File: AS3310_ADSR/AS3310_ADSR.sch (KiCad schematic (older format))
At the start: 26 parts, among them J1 ADSR_Pots, J2 Gate, J3 Peak, J4 AtkOut, J5 EnvOut, J6 Trigger, J7 Power, U1 AS3310, U2 TL071

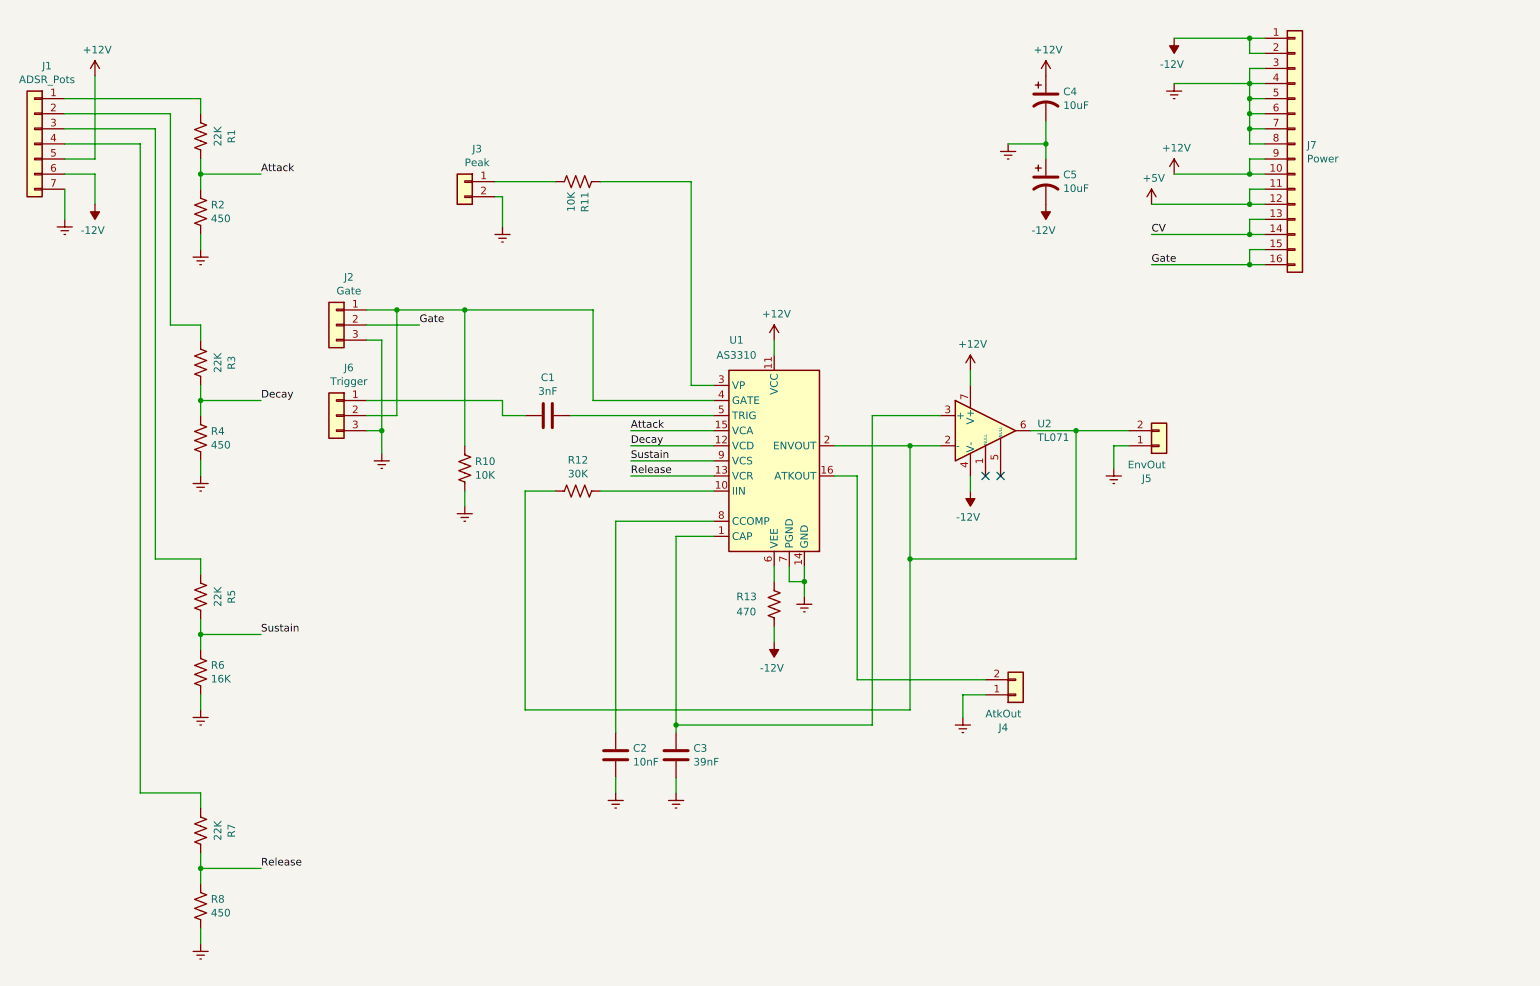
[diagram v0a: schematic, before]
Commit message: Combine IO and main ADSR boards
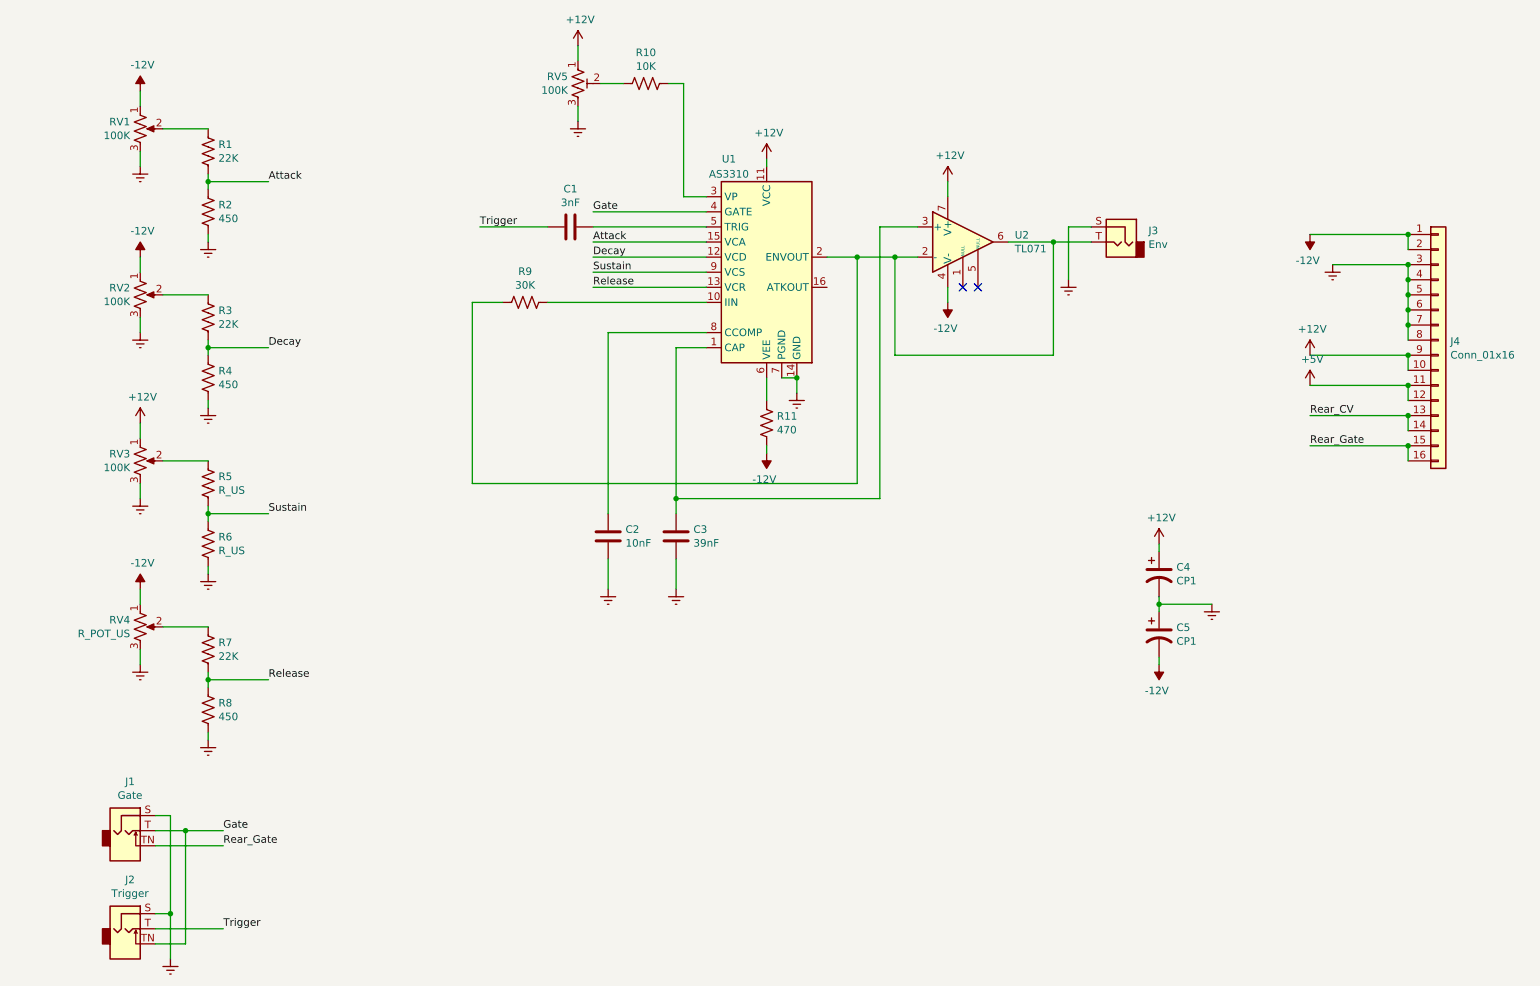
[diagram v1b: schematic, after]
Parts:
- removed J1: ADSR_Pots, Connector_PinHeader_2.54mm:PinHeader_1x07_P2.54mm_Vertical, symbol Connector_Generic:Conn_01x07
- removed J2: Gate, Connector_PinHeader_2.54mm:PinHeader_1x03_P2.54mm_Vertical, symbol Connector_Generic:Conn_01x03
- removed J3: Peak, Connector_PinHeader_2.54mm:PinHeader_1x02_P2.54mm_Vertical, symbol Connector_Generic:Conn_01x02
- removed J4: AtkOut, Connector_PinHeader_2.54mm:PinHeader_1x02_P2.54mm_Vertical, symbol Connector_Generic:Conn_01x02
- removed J5: EnvOut, Connector_PinHeader_2.54mm:PinHeader_1x02_P2.54mm_Vertical, symbol Connector_Generic:Conn_01x02
- removed J6: Trigger, Connector_PinHeader_2.54mm:PinHeader_1x03_P2.54mm_Vertical, symbol Connector_Generic:Conn_01x03
- removed J7: Power, Connector_IDC:IDC-Header_2x08_P2.54mm_Vertical, symbol Connector_Generic:Conn_01x16
- removed R12: 30K, Resistor_SMD:R_0805_2012Metric, symbol Device:R_US
- removed R13: 470, Resistor_SMD:R_0805_2012Metric, symbol Device:R_US
- added J1: Gate, Eurorack:Jack_3.5mm_QingPu_WQP-PJ398SM_Vertical_CircularHoles, symbol Connector:AudioJack2_SwitchT
- added J2: Trigger, Eurorack:Jack_3.5mm_QingPu_WQP-PJ398SM_Vertical_CircularHoles, symbol Connector:AudioJack2_SwitchT
- added J3: Env, Eurorack:Jack_3.5mm_QingPu_WQP-PJ398SM_Vertical_CircularHoles, symbol Connector:AudioJack2
- added J4: Conn_01x16, Connector_IDC:IDC-Header_2x08_P2.54mm_Vertical, symbol Connector_Generic:Conn_01x16
- added R9: 30K, Resistor_SMD:R_0805_2012Metric, symbol Device:R_US
- added RV1, RV2, RV3: 100K, Eurorack:Potentiometer_TT_P0915N, symbol Device:R_POT_US
- added RV4: R_POT_US, Eurorack:Potentiometer_TT_P0915N, symbol Device:R_POT_US
- added RV5: 100K, Potentiometer_THT:Potentiometer_Bourns_3296W_Vertical, symbol Device:R_POT_TRIM_US
- C4, C5: value 10uF -> CP1
- R11: value 10K -> 470
- R5: value 22K -> R_US
- R6: value 16K -> R_US
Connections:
- net +12V: now also J4.10 (Pin_10), J4.9 (Pin_9), RV3.1, RV5.1
- net +5V: now also J4.11 (Pin_11), J4.12 (Pin_12)
- net -12V: now also R11.2, J4.1 (Pin_1), J4.2 (Pin_2), RV1.1, RV2.1, RV4.1
- net Attack: now also R1.2, R2.1; no longer R1.1, R2.2
- net Decay: now also R3.2, R4.1; no longer R3.1, R4.2
- net GNDREF: now also R2.2, R4.2, R6.2, R8.2, J1.S, J2.S, J3.S, J4.3 (Pin_3), J4.4 (Pin_4), J4.5 (Pin_5), J4.6 (Pin_6), J4.7 (Pin_7), J4.8 (Pin_8), RV1.3, RV2.3, RV3.3, RV4.3, RV5.3; no longer R10.1, R2.1, R4.1, R6.1, R8.1
- net Gate: now also U1.4 (GATE), J1.T, J2.TN
- net Release: now also R7.2, R8.1; no longer R7.1, R8.2
- net Sustain: now also R5.2, R6.1; no longer R5.1, R6.2
- net at U1.10 (IIN): now also R9.1
- net at U1.2 (ENVOUT), U2.2 (-), U2.6: now also J3.T, R9.2
- net at U1.3 (VP): now also R10.1; no longer R11.2
- net at R10.2: now also RV5.2; no longer U1.4 (GATE)
- net at U1.6 (VEE): now also R11.1
- net Trigger: now reaches C1.2
- net Trigger: now also J2.T
- new net: R1.1, RV1.2
- new net: R3.1, RV2.2
- new net: R5.1, RV3.2
- new net: R7.1, RV4.2
- new net Rear_CV: J4.13 (Pin_13), J4.14 (Pin_14)
- new net Rear_Gate: J1.TN, J4.15 (Pin_15), J4.16 (Pin_16)
